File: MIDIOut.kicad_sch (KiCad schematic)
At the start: 6 parts, among them J201 SJ2-25504B-SMT-TR, U201 TLP2361

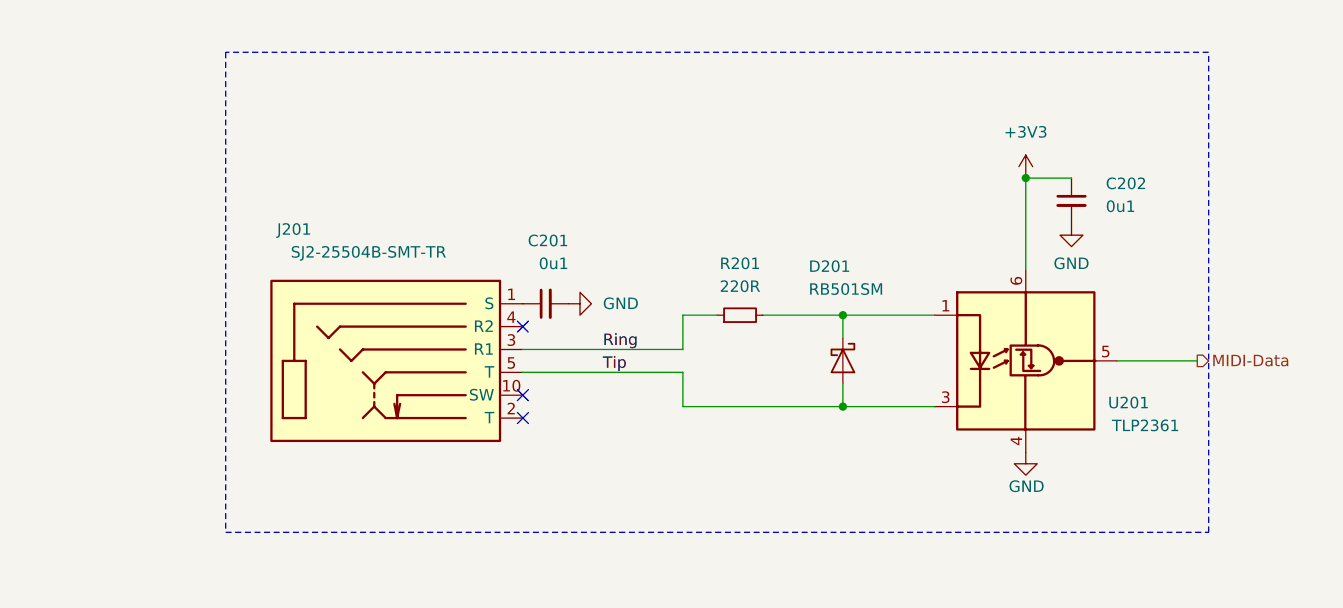
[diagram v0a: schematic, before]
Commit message: Replace MIDI In with MIDI Out
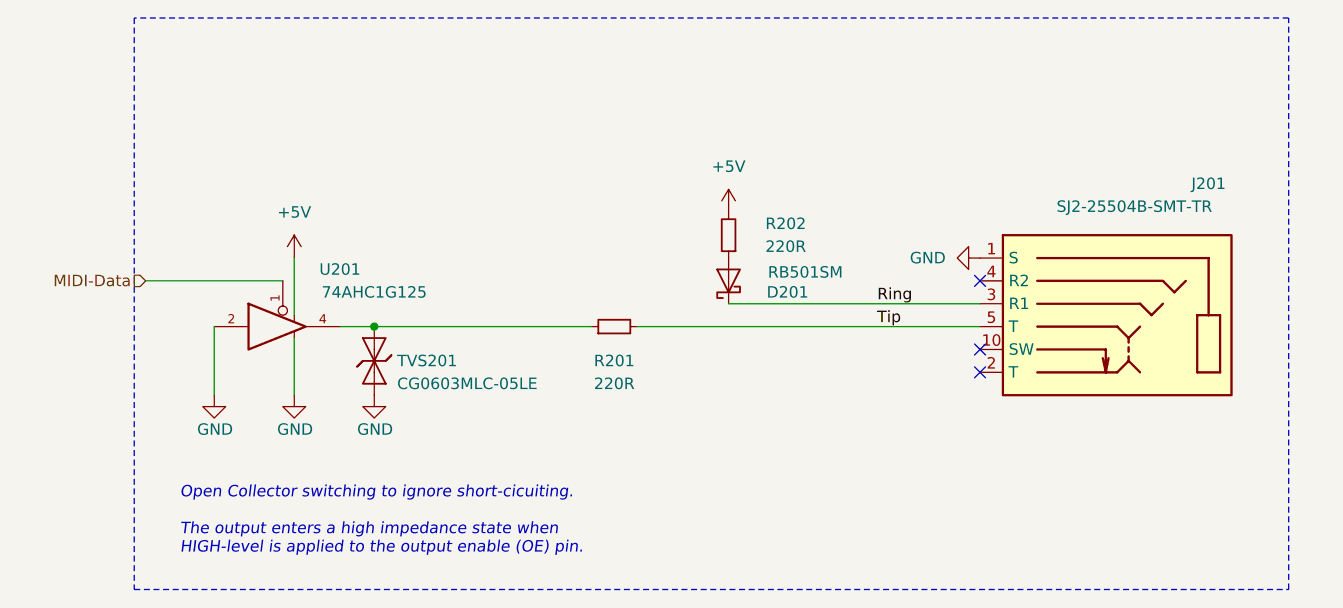
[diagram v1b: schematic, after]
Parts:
- removed C201, C202: 0u1, Capacitor_SMD:C_0603_1608Metric, symbol Device:C_Small
- removed U201: TLP2361, Package_SO:SO-6_4.4x3.6mm_P1.27mm, symbol V2_Isolator:TLP2361
- added R202: 220R, Resistor_SMD:R_0603_1608Metric, symbol Device:R_Small
- added TVS201: CG0603MLC-05LE, Diode_SMD:D_0603_1608Metric, symbol V2_Diode:CG0603MLC-05LE
- added U201: 74AHC1G125, Package_TO_SOT_SMD:SOT-23-5, symbol V2_74xGxx:74AHC1G125
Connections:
- net GND: now also J201.1 (S), TVS201.1 (K), U201.2, U201.3
- net MIDI-Data: now also U201.1
- net Ring: now also D201.1 (K); no longer R201.1
- net Tip: now also R201.2; no longer D201.2 (A)
- new net: R201.1, TVS201.2 (A), U201.4
- new net: D201.2 (A), R202.1
- new net +5V: R202.2, U201.5
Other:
- note added: "﻿Open Collector switching to ignore short-cicuiting. The output enters a high impedance state when HIGH-level is applied to the output enable (OE) pin."
- title: MIDI In -> MIDI Out
- moved on the sheet: D201, J201, R201
